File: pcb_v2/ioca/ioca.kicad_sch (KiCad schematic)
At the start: 65 parts, among them J1 bus ioc 1, J10 in f2, J11 in f3, J12 serial0, J13 serial0, J2 bus ioc 2, J3 bus ioc 3, J4 out f0, J5 out f1, J6 out f2, J7 out f3, J8 in f0, J9 in f1, U1 74HC238, U10 74LS574, U11 74LS574, U12 MC14495P, U13 F4_LOW, U14 MC14495P, U15 F4_HIGH, U16 74LS574, U17 MC14495P, U18 F5_LOW, U19 MC14495P, U2 74LS138, U20 F5_HIGH, U21 74LS244, U22 74LS244, U23 74LS244, U24 74LS244, U25 74LS574, U26 74LS244, U27 74LS574, U28 74LS244, U3 74LS138, U4 74HC238, U5 74LS138, U6 74LS138, U7 74LS574, U8 74LS574, U9 74LS574

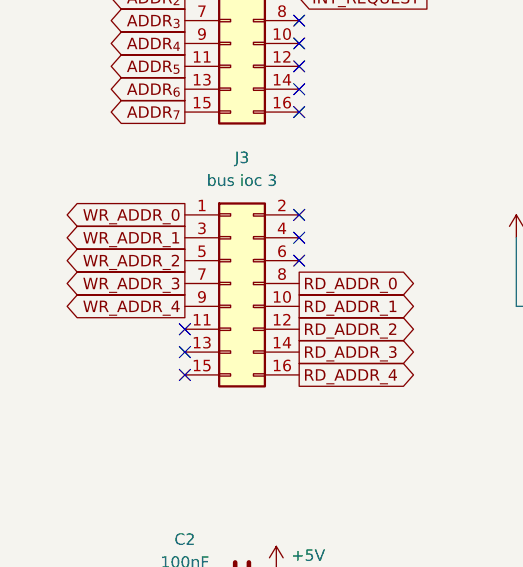
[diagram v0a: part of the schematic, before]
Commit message: padronização de conector de IO; ideias para o layout do backplane
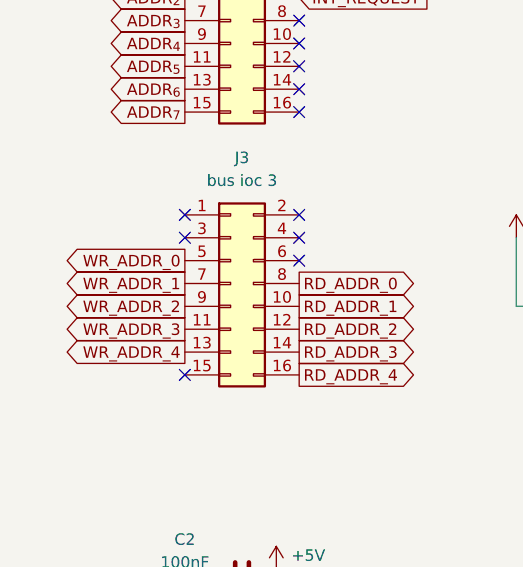
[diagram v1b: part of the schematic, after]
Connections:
- net WR_ADDR_0: now also J3.5 (Pin_5); no longer J3.1 (Pin_1)
- net WR_ADDR_1: now also J3.7 (Pin_7); no longer J3.3 (Pin_3)
- net WR_ADDR_2: now also J3.9 (Pin_9); no longer J3.5 (Pin_5)
- net WR_ADDR_3: now also J3.11 (Pin_11); no longer J3.7 (Pin_7)
- net WR_ADDR_4: now also J3.13 (Pin_13); no longer J3.9 (Pin_9)
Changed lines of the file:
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@@
 	)
 	(no_connect
+		(at 27.94 81.28)
+	)
+	(no_connect
 		(at 40.64 64.77)
 	)
@@
 	)
 	(no_connect
-		(at 27.94 93.98)
-	)
-	(no_connect
 		(at 50.8 140.97)
 	)
@@
 	)
 	(no_connect
-		(at 27.94 96.52)
+		(at 27.94 83.82)
 	)
 	(no_connect
@@
 		)
 	)
+	(global_label "WR_ADDR_3"
+		(shape output)
+		(at 27.94 93.98 180)
+		(fields_autoplaced yes)
+		(effects
+			(font
+				(size 1.27 1.27)
+			)
+			(justify right)
+		)
+		(property "Intersheetrefs" "${INTERSHEET_REFS}"
+			(at 14.1901 93.98 0)
+			(effects
+				(font
+					(size 1.27 1.27)
+				)
+				(justify right)
+				(hide yes)
+			)
+		)
+	)
 	(global_label "DATA_{0}"
 		(shape input)
@@
 		)
 	)
-	(global_label "WR_ADDR_1"
-		(shape output)
-		(at 27.94 83.82 180)
-		(fields_autoplaced yes)
-		(effects
-			(font
-				(size 1.27 1.27)
-			)
-			(justify right)
-		)
-		(property "Intersheetrefs" "${INTERSHEET_REFS}"
-			(at 14.1901 83.82 0)
-			(effects
-				(font
-					(size 1.27 1.27)
-				)
-				(justify right)
-				(hide yes)
-			)
-		)
-	)
 	(global_label "serial0_out_1"
 		(shape input)
@@
 		)
 	)
-	(global_label "WR_ADDR_3"
-		(shape output)
-		(at 27.94 88.9 180)
-		(fields_autoplaced yes)
-		(effects
-			(font
-				(size 1.27 1.27)
-			)
-			(justify right)
-		)
-		(property "Intersheetrefs" "${INTERSHEET_REFS}"
-			(at 14.1901 88.9 0)
-			(effects
-				(font
-					(size 1.27 1.27)
-				)
-				(justify right)
-				(hide yes)
-			)
-		)
-	)
 	(global_label "DATA_{3}"
 		(shape input)
@@
 		)
 	)
-	(global_label "WR_ADDR_2"
+	(global_label "WR_ADDR_1"
 		(shape output)
-		(at 27.94 86.36 180)
+		(at 27.94 88.9 180)
 		(fields_autoplaced yes)
 		(effects
@@
 		)
 		(property "Intersheetrefs" "${INTERSHEET_REFS}"
-			(at 14.1901 86.36 0)
+			(at 14.1901 88.9 0)
 			(effects
 				(font
@@
 		)
 	)
-	(global_label "WR_ADDR_4"
-		(shape output)
-		(at 27.94 91.44 180)
-		(fields_autoplaced yes)
-		(effects
-			(font
-				(size 1.27 1.27)
-			)
-			(justify right)
-		)
-		(property "Intersheetrefs" "${INTERSHEET_REFS}"
-			(at 14.1901 91.44 0)
-			(effects
-				(font
-					(size 1.27 1.27)
-				)
-				(justify right)
-				(hide yes)
-			)
-		)
-	)
 	(global_label "serial1_out_5"
 		(shape input)
@@
 		)
 	)
-	(global_label "WR_ADDR_0"
-		(shape output)
-		(at 27.94 81.28 180)
-		(fields_autoplaced yes)
-		(effects
-			(font
-				(size 1.27 1.27)
-			)
-			(justify right)
-		)
-		(property "Intersheetrefs" "${INTERSHEET_REFS}"
-			(at 14.1901 81.28 0)
-			(effects
-				(font
-					(size 1.27 1.27)
-				)
-				(justify right)
-				(hide yes)
-			)
-		)
-	)
 	(global_label "DATA_{5}"
 		(shape output)
@@
 		)
 	)
+	(global_label "WR_ADDR_4"
+		(shape output)
+		(at 27.94 96.52 180)
+		(fields_autoplaced yes)
+		(effects
+			(font
+				(size 1.27 1.27)
+			)
+			(justify right)
+		)
+		(property "Intersheetrefs" "${INTERSHEET_REFS}"
+			(at 14.1901 96.52 0)
+			(effects
+				(font
+					(size 1.27 1.27)
+				)
+				(justify right)
+				(hide yes)
+			)
+		)
+	)
 	(global_label "serial1_out_4"
 		(shape input)
@@
 		)
 	)
+	(global_label "WR_ADDR_2"
+		(shape output)
+		(at 27.94 91.44 180)
+		(fields_autoplaced yes)
+		(effects
+			(font
+				(size 1.27 1.27)
+			)
+			(justify right)
+		)
+		(property "Intersheetrefs" "${INTERSHEET_REFS}"
+			(at 14.1901 91.44 0)
+			(effects
+				(font
+					(size 1.27 1.27)
+				)
+				(justify right)
+				(hide yes)
+			)
+		)
+	)
 	(global_label "~{in_port_f6}"
 		(shape input)
@@
 				(hide yes)
 			)
+		)
+	)
+	(global_label "WR_ADDR_0"
+		(shape output)
+		(at 27.94 86.36 180)
+		(fields_autoplaced yes)
+		(effects
+			(font
+				(size 1.27 1.27)
+			)
+			(justify right)
+		)
+		(property "Intersheetrefs" "${INTERSHEET_REFS}"
+			(at 14.1901 86.36 0)
+			(effects
+				(font
+					(size 1.27 1.27)
+				)
+				(justify right)
+				(hide yes)
+			)
